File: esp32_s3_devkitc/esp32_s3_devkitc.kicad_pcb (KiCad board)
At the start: 2 copper layers, 30 x 63 mm, 51 parts, among them J1 Conn_01x22, J2 Conn_01x22, J3 Micro USB (UART), J4 Micro USB (NATIVE USB), Q1 L8050QLT1G, Q2 L8050QLT1G, U1 ESP32-S3-WROOM-1, U2 CP2102N-Axx-xQFN28, U3 SGM2212-3.3

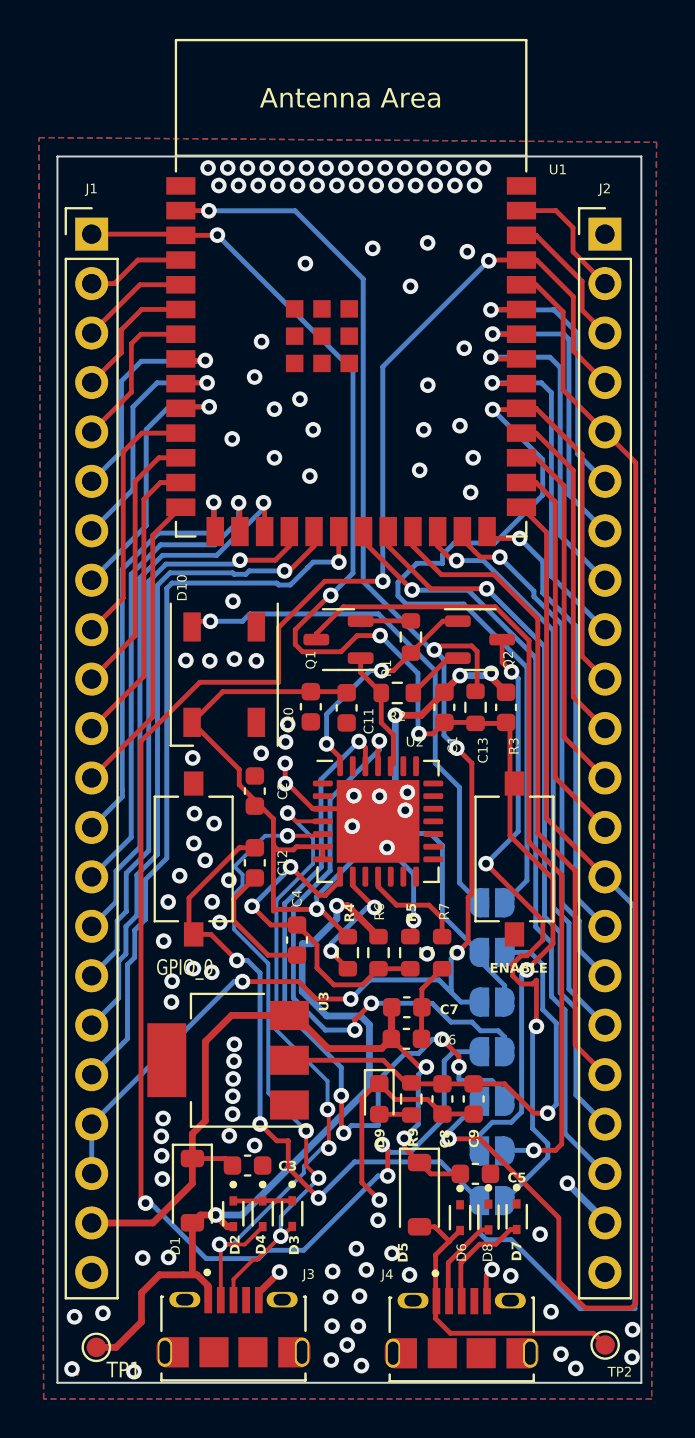
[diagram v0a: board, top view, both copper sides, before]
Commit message: fix de componentes desconectados y reodenamiento de vias
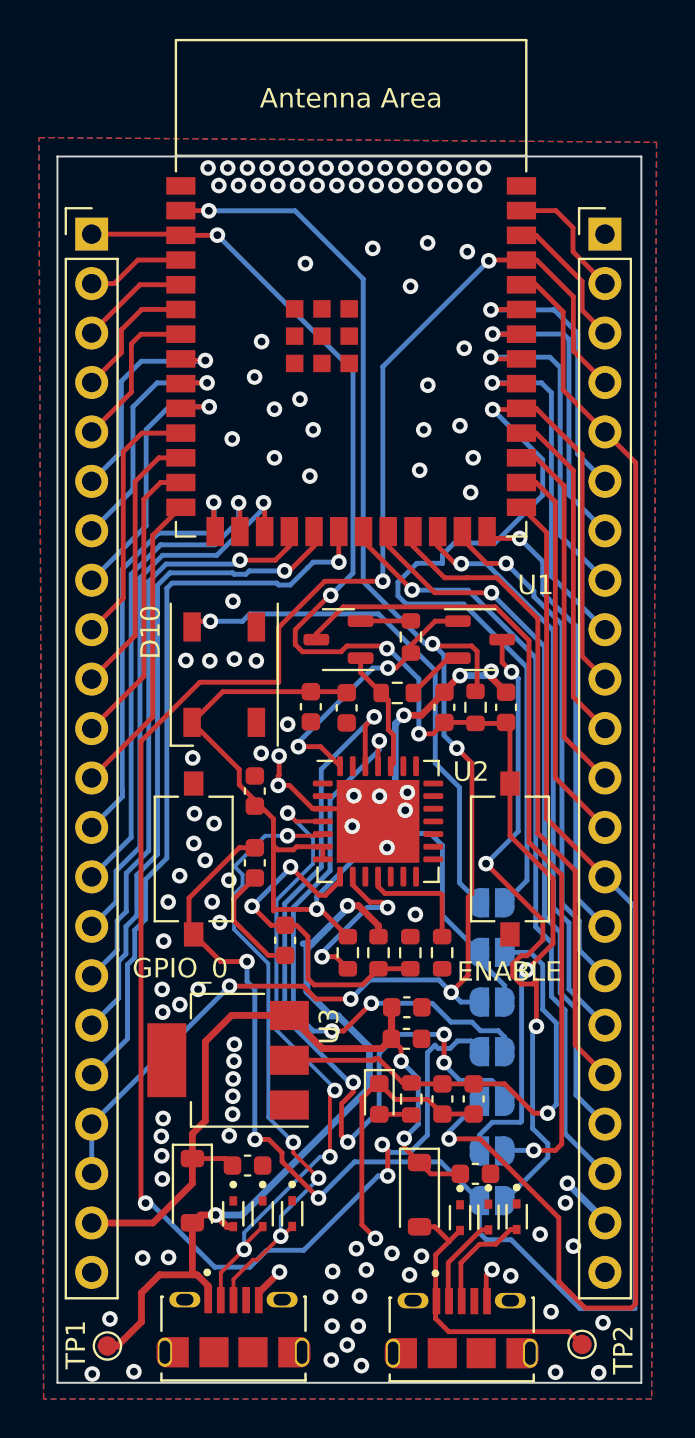
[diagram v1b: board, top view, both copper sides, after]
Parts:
- JP3: value U0RXD -> RXD
- JP4: value U0TXD -> TXD
- moved TP2 1.19 mm to (136.9, 101.0)
- moved C4 0.61 mm to (121.7, 80.3)
- moved TP1 0.57 mm to (112.6, 101.1)
- moved ENABLE 0.23 mm to (133.2, 76.1)
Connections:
- J4 pad S1: (no net) -> GND
- J4 pad S2: (no net) -> GND
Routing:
- net GND: track 57.1 -> 46.3 mm, vias 126 -> 123
- net Net-(JP3-A): track 38.3 -> 43.1 mm
- net Net-(U2-~{RST}): track 6.69 -> 8.81 mm
- net /bridge-uart/DTR: track 11.7 -> 13.8 mm
- net /bridge-uart/U0TXD: track 96.4 -> 98.2 mm
- net /bridge-uart/VBUS: track 40.6 -> 39.2 mm
- net Net-(D5-A): track 16.2 -> 15.0 mm
- net /bridge-uart/USB_DP: track 35.1 -> 34.0 mm
- net Net-(U2-~{SUSPEND}): track 5.42 -> 6.12 mm
- net Net-(U2-VBUS): track 17.3 -> 17.9 mm
